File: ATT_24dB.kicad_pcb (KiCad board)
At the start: 2 copper layers, 54 x 33 mm, 24 parts, among them J1 SMAJ-TX, J2 SMAJ-ANT

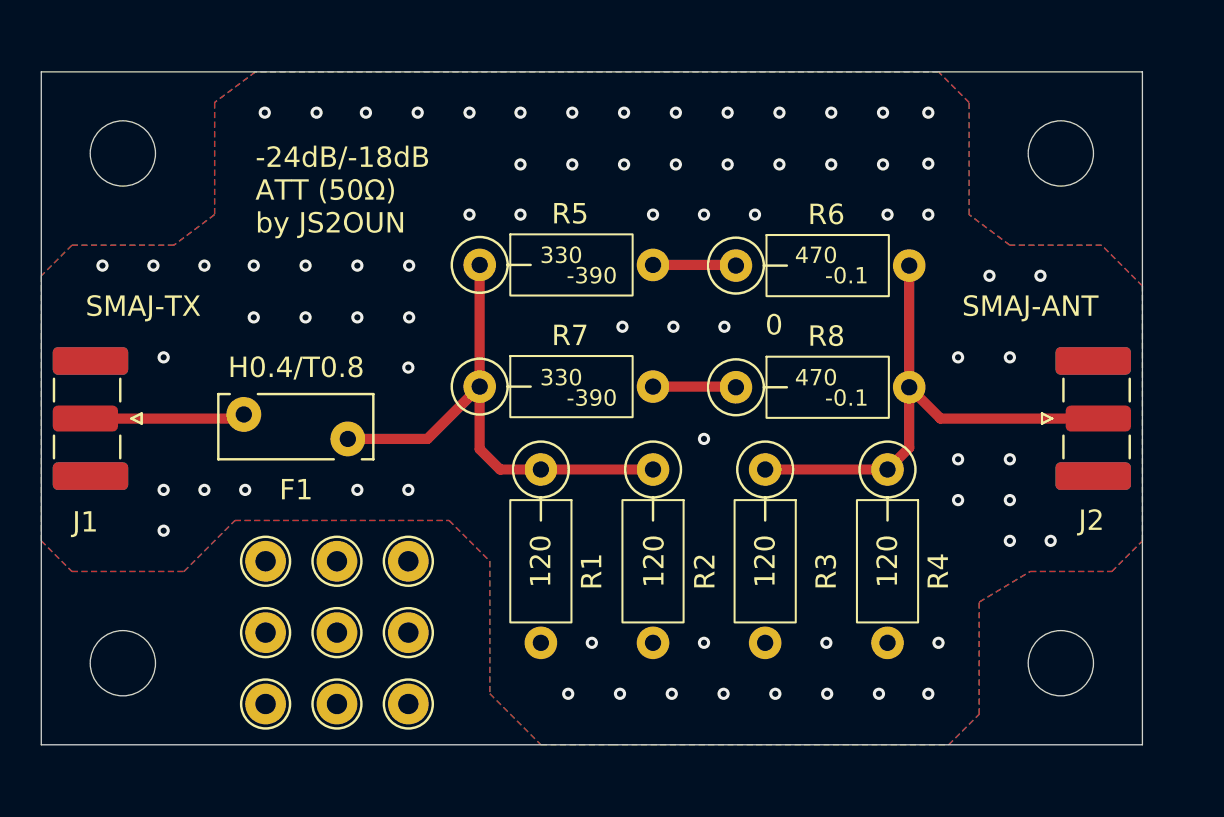
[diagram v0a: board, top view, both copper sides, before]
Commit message: SMA端子のセンターずれ対策
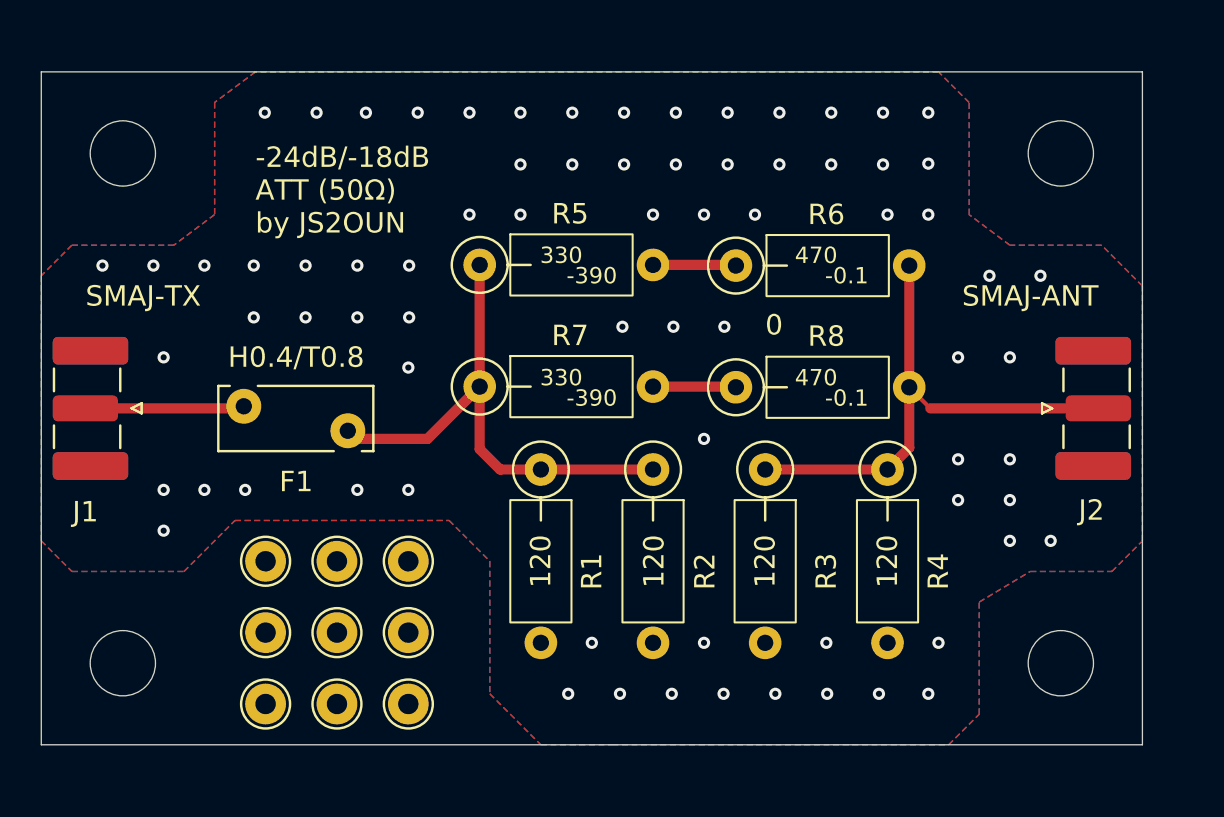
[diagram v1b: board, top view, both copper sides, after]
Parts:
- moved J1 0.50 mm to (62.7, 41.5)
- moved J2 0.50 mm to (112.3, 41.5)
- moved F1 0.40 mm to (75.5, 42.6)
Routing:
- net Net-(J2-In): track 28.1 -> 26.9 mm
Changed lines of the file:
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@@
 	(footprint "Connector_Coaxial:SMA_Samtec_SMA-J-P-H-ST-EM1_EdgeMount"
 		(layer "F.Cu")
-		(at 112.3375 42)
+		(at 112.3375 41.5)
 		(descr "Connector SMA, 0Hz to 20GHz, 50Ohm, Edge Mount (http://suddendocs.samtec.com/prints/sma-j-p-x-st-em1-mkt.pdf)")
 		(tags "SMA Straight Samtec Edge Mount")
@@
 	(footprint "Connector_Coaxial:SMA_Samtec_SMA-J-P-H-ST-EM1_EdgeMount"
 		(layer "F.Cu")
-		(at 62.6625 42 180)
+		(at 62.6625 41.5 180)
 		(descr "Connector SMA, 0Hz to 20GHz, 50Ohm, Edge Mount (http://suddendocs.samtec.com/prints/sma-j-p-x-st-em1-mkt.pdf)")
 		(tags "SMA Straight Samtec Edge Mount")
@@
 	(footprint "X_FUSE_THT:Fuse_Bourns_MF-R010_040"
 		(layer "F.Cu")
-		(at 75.5325 43 180)
+		(at 75.5325 42.6 180)
 		(descr "PTC Resettable Fuse, Ihold = 0.40A, Itrip=0.80A, https://akizukidenshi.com/goodsaffix/mfr.pdf")
 		(tags "ptc resettable fuse polyfuse THT")
@@
 		)
 		(property "Value" "H0.4/T0.8"
-			(at 2.5325 3.5 180)
+			(at 2.5325 3.6 180)
 			(layer "F.SilkS")
 			(effects
@@
 		)
 		(height -4.5)
-		(gr_text "2125.9843 mils"
+		(gr_text "54.0000 mm"
 			(at 87.5 18.7 0)
 			(layer "F.Cu")
@@
 		)
 		(height -16.5)
-		(gr_text "1299.2126 mils"
+		(gr_text "33.0000 mm"
 			(at 129.2 41.5 90)
 			(layer "F.Cu")
@@
 		)
 		(height 8)
-		(gr_text "1811.0236 mils"
+		(gr_text "46.0000 mm"
 			(at 87.5 60.85 0)
 			(layer "Cmts.User")
@@
 		)
 		(height 17.5)
-		(gr_text "984.2520 mils"
+		(gr_text "25.0000 mm"
 			(at 45.85 41.5 90)
 			(layer "Cmts.User")
@@
 	)
 	(segment
+		(start 70.3325 41.5)
+		(end 70.4325 41.4)
+		(width 0.2)
+		(layer "F.Cu")
+		(net 2)
+	)
+	(segment
 		(start 70.2325 42)
 		(end 70.4325 41.8)
@@
 	)
 	(segment
-		(start 62.6625 42)
-		(end 70.2325 42)
+		(start 62.6625 41.5)
+		(end 70.3325 41.5)
 		(width 0.5)
 		(layer "F.Cu")
@@
 	)
 	(segment
-		(start 104.5975 42)
-		(end 103.065 40.4675)
+		(start 112.3375 41.5)
+		(end 104.0975 41.5)
 		(width 0.5)
 		(layer "F.Cu")
@@
 	)
 	(segment
-		(start 113.3375 42)
-		(end 104.5975 42)
-		(width 0.5)
+		(start 104.0975 41.5)
+		(end 103.065 40.4675)
+		(width 0.2)
 		(layer "F.Cu")
 		(net 4)

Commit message: SW-65筐体に適合するよう、エッジカットを修正
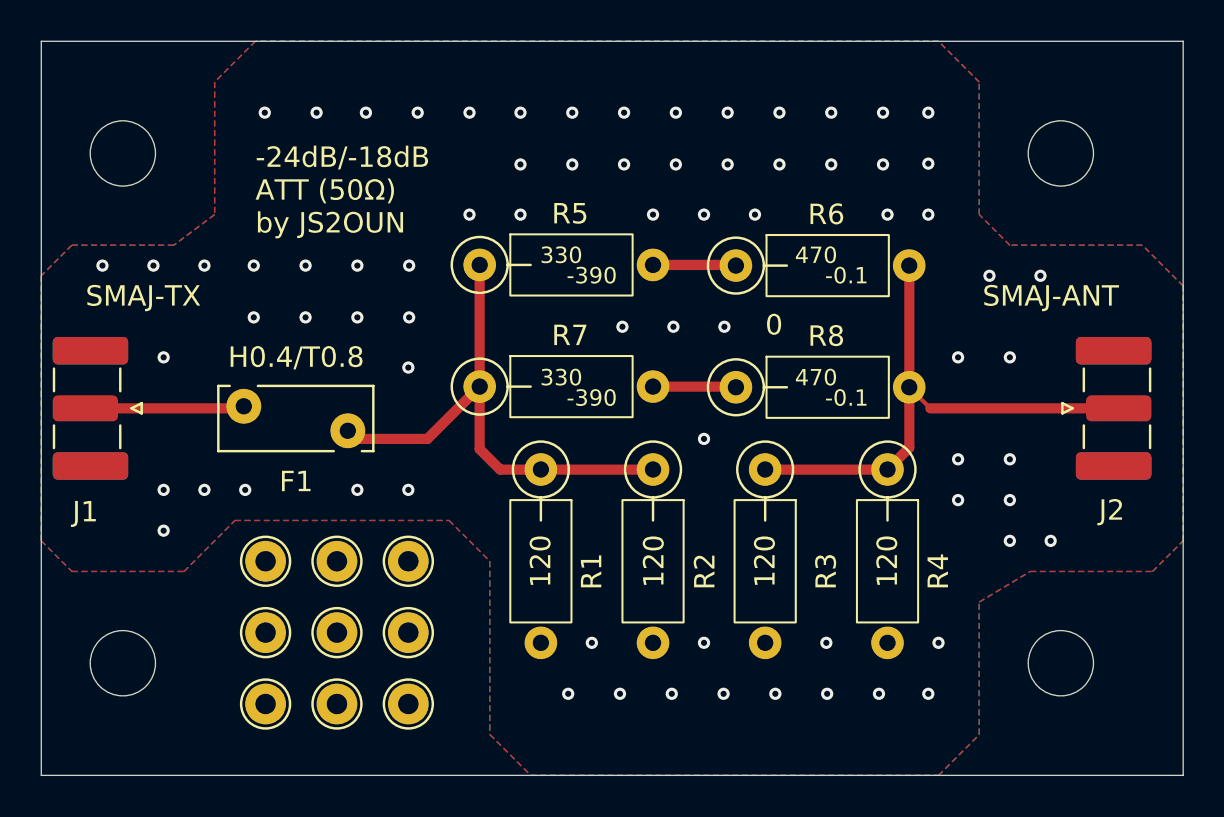
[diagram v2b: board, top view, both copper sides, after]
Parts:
- moved J2 1.00 mm to (113.3, 41.5)
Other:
- board size 54 x 33 mm -> 56 x 36 mm
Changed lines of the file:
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@@
 	(footprint "Connector_Coaxial:SMA_Samtec_SMA-J-P-H-ST-EM1_EdgeMount"
 		(layer "F.Cu")
-		(at 112.3375 41.5)
+		(at 113.3375 41.5)
 		(descr "Connector SMA, 0Hz to 20GHz, 50Ohm, Edge Mount (http://suddendocs.samtec.com/prints/sma-j-p-x-st-em1-mkt.pdf)")
 		(tags "SMA Straight Samtec Edge Mount")
@@
 	)
 	(gr_rect
-		(start 60.5 25)
-		(end 114.5 58)
+		(start 60.5 23.5)
+		(end 116.5 59.5)
 		(stroke
 			(width 0.05)
@@
 		(layer "F.Cu")
 		(pts
-			(xy 60.5 25) (xy 114.5 25)
+			(xy 60.5 23.5) (xy 116.5 23.5)
 		)
 		(height -4.5)
-		(gr_text "54.0000 mm"
-			(at 87.5 18.7 0)
+		(gr_text "56.0000 mm"
+			(at 88.5 17.2 0)
 			(layer "F.Cu")
 			(effects
@@
 		(layer "F.Cu")
 		(pts
-			(xy 114.5 25) (xy 114.5 58)
+			(xy 116.5 23.5) (xy 116.5 59.5)
 		)
 		(height -16.5)
-		(gr_text "33.0000 mm"
-			(at 129.2 41.5 90)
+		(gr_text "36.0000 mm"
+			(at 131.2 41.5 90)
 			(layer "F.Cu")
 			(effects
@@
 		(polygon
 			(pts
-				(xy 113 49.5) (xy 114.5 48) (xy 114.5 35.5) (xy 112.5 33.5) (xy 108 33.5) (xy 106 32) (xy 106 26.5)
-				(xy 104.5 25) (xy 71 25) (xy 69 26.5) (xy 69 32) (xy 67 33.5) (xy 62 33.5) (xy 60.5 35) (xy 60.5 48)
-				(xy 62 49.5) (xy 67.5 49.5) (xy 70 47) (xy 80.5 47) (xy 82.5 49) (xy 82.5 55.5) (xy 85 58) (xy 88.5 58)
-				(xy 105 58) (xy 106.5 56.5) (xy 106.5 51) (xy 109 49.5)
+				(xy 115 49.5) (xy 116.5 48) (xy 116.5 35.5) (xy 114.5 33.5) (xy 108 33.5) (xy 106.5 32) (xy 106.5 25.5)
+				(xy 104.5 23.5) (xy 71 23.5) (xy 69 25.5) (xy 69 32) (xy 67 33.5) (xy 62 33.5) (xy 60.5 35) (xy 60.5 48)
+				(xy 62 49.5) (xy 67.5 49.5) (xy 70 47) (xy 80.5 47) (xy 82.5 49) (xy 82.5 57.5) (xy 84.5 59.5) (xy 104.5 59.5)
+				(xy 106.5 57.5) (xy 106.5 51) (xy 109 49.5)
 			)
 		)
